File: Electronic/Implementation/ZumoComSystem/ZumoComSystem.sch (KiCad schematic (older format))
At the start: 1 part

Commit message: #95 START Hardware-Version v1.2 - L2: pad size increased - some small fixes
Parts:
- renumbered L1 to Logo1
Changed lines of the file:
@@
 Sheet 1 7
 Title "Zumo Communication System"
-Date "2022-08-11"
-Rev "V1.1"
+Date "2022-09-05"
+Rev "V1.2"
 Comp "NewTec GmbH"
 Comment1 "Schneider, Niklas"
@@
 $EndBitmap
 $Comp
-L NewTec_Logo:NewTec_Logo L1
+L NewTec_Logo:NewTec_Logo Logo1
 U 1 1 62F4D7EF
 P 750 7700
-F 0 "L1" H 750 7800 50  0001 C CNN
+F 0 "Logo1" H 750 7800 50  0001 C CNN
 F 1 "NewTec_Logo" H 750 7700 50  0000 C CNN
 F 2 "footprints:NT_Kicad_Logo_2500x2500" H 750 7700 50  0001 C CNN

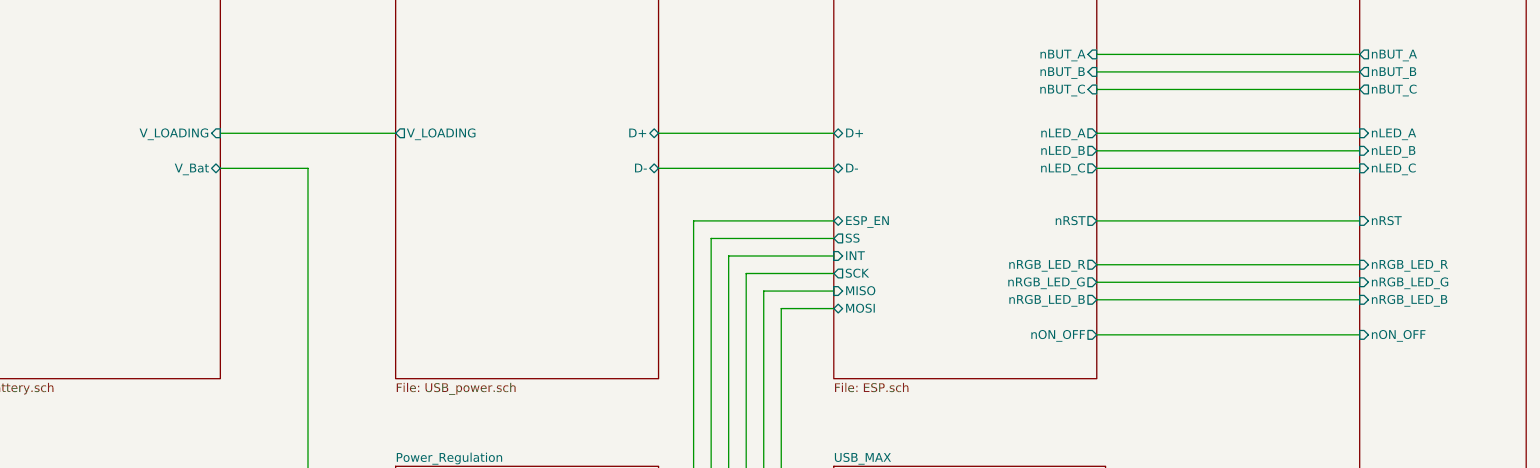
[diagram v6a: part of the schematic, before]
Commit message: #95 Connection between LEDs A, B and C and the ESP removed and mirrored by the Zumo robot instead
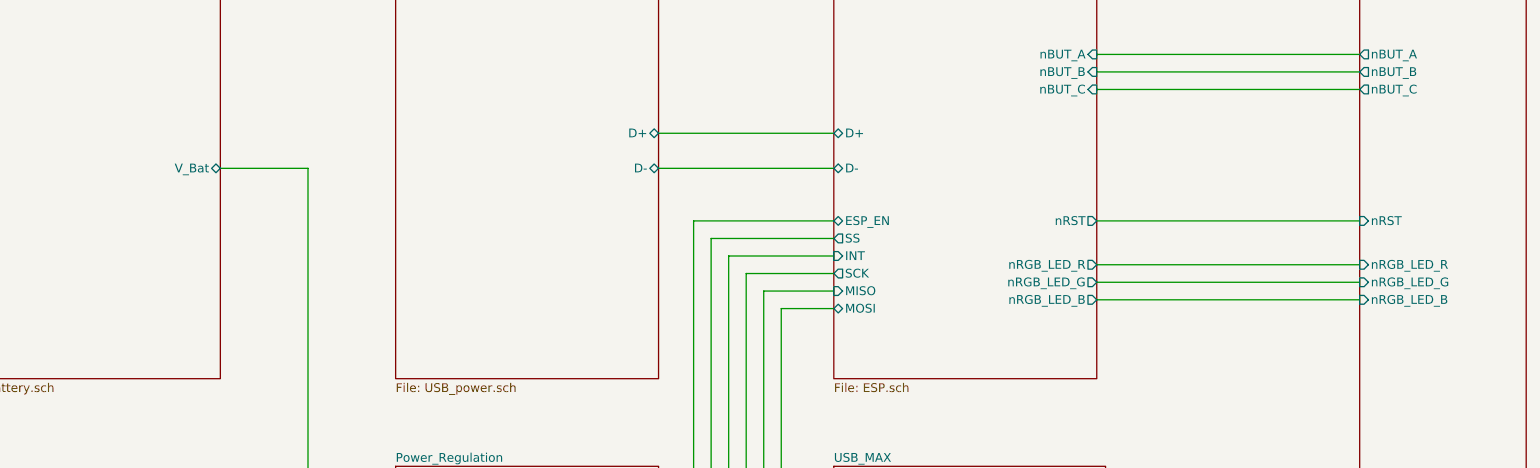
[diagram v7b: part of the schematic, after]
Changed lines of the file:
@@
 Sheet 1 7
 Title "Zumo Communication System"
-Date "2022-10-04"
+Date "2022-10-07"
 Rev "V1.2"
 Comp "NewTec GmbH"
@@
 F1 "battery.sch" 50
 F2 "V_Bat" B R 3000 2100 50
-F3 "V_LOADING" I R 3000 1900 50
 $EndSheet
 Wire Wire Line
@@
 Wire Wire Line
 	9500 1650 8000 1650
-Wire Wire Line
-	9500 2000 8000 2000
-Wire Wire Line
-	8000 1900 9500 1900
-Wire Wire Line
-	8000 2100 9500 2100
 Wire Wire Line
 	8000 2400 9500 2400
@@
 F2 "D-" B R 5500 2100 50
 F3 "D+" B R 5500 1900 50
-F4 "V_LOADING" O L 4000 1900 50
 $EndSheet
 Wire Wire Line
@@
 F7 "D+" B L 6500 1900 50
 F8 "D-" B L 6500 2100 50
-F9 "nLED_A" O R 8000 1900 50
-F10 "nLED_B" O R 8000 2000 50
-F11 "nLED_C" O R 8000 2100 50
-F12 "nRGB_LED_R" O R 8000 2650 50
-F13 "nRGB_LED_G" O R 8000 2750 50
-F14 "nRGB_LED_B" O R 8000 2850 50
-F15 "nRST" O R 8000 2400 50
-F16 "nON_OFF" O R 8000 3050 50
-F17 "nBUT_B" I R 8000 1550 50
-F18 "nBUT_C" I R 8000 1650 50
-F19 "nBUT_A" I R 8000 1450 50
-F20 "ESP_EN" B L 6500 2400 50
+F9 "nRGB_LED_R" O R 8000 2650 50
+F10 "nRGB_LED_G" O R 8000 2750 50
+F11 "nRGB_LED_B" O R 8000 2850 50
+F12 "nRST" O R 8000 2400 50
+F13 "nBUT_B" I R 8000 1550 50
+F14 "nBUT_C" I R 8000 1650 50
+F15 "nBUT_A" I R 8000 1450 50
+F16 "ESP_EN" B L 6500 2400 50
 $EndSheet
-Wire Wire Line
-	9500 3050 8000 3050
-Wire Wire Line
-	3000 1900 4000 1900
 $Bitmap
 Pos 10450 6750
@@
 F0 "IF_Pololu" 50
 F1 "IF_pololu.sch" 50
-F2 "nLED_B" I L 9500 2000 50
-F3 "nLED_C" I L 9500 2100 50
-F4 "nLED_A" I L 9500 1900 50
-F5 "nRGB_LED_R" I L 9500 2650 50
-F6 "nRGB_LED_G" I L 9500 2750 50
-F7 "nRGB_LED_B" I L 9500 2850 50
-F8 "nRST" I L 9500 2400 50
-F9 "nON_OFF" I L 9500 3050 50
-F10 "nBUT_C" O L 9500 1650 50
-F11 "nBUT_B" O L 9500 1550 50
-F12 "nBUT_A" O L 9500 1450 50
+F2 "nRGB_LED_R" I L 9500 2650 50
+F3 "nRGB_LED_G" I L 9500 2750 50
+F4 "nRGB_LED_B" I L 9500 2850 50
+F5 "nRST" I L 9500 2400 50
+F6 "nBUT_C" O L 9500 1650 50
+F7 "nBUT_B" O L 9500 1550 50
+F8 "nBUT_A" O L 9500 1450 50
 $EndSheet
 Wire Wire Line
